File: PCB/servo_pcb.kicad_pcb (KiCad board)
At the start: 2 copper layers, 35 x 16 mm, 42 parts, among them J1 power in, M1 M1, M2 M2, U1 MM32G0001, U2 SL7533-3, U3 BDR6121H, U4 INA180A2, U5 AS5600

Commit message: cleaned up older pcbs and updated the master pcb
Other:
- board text added: "μDrive_1.0"
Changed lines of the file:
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@@
+		)
+	)
+	(gr_text "μDrive_1.0\n"
+		(at 75.5 33.6 0)
+		(layer "B.SilkS")
+		(effects
+			(font
+				(size 1.5 1.5)
+				(thickness 0.2)
+			)
+			(justify left bottom mirror)
 		)
 	)

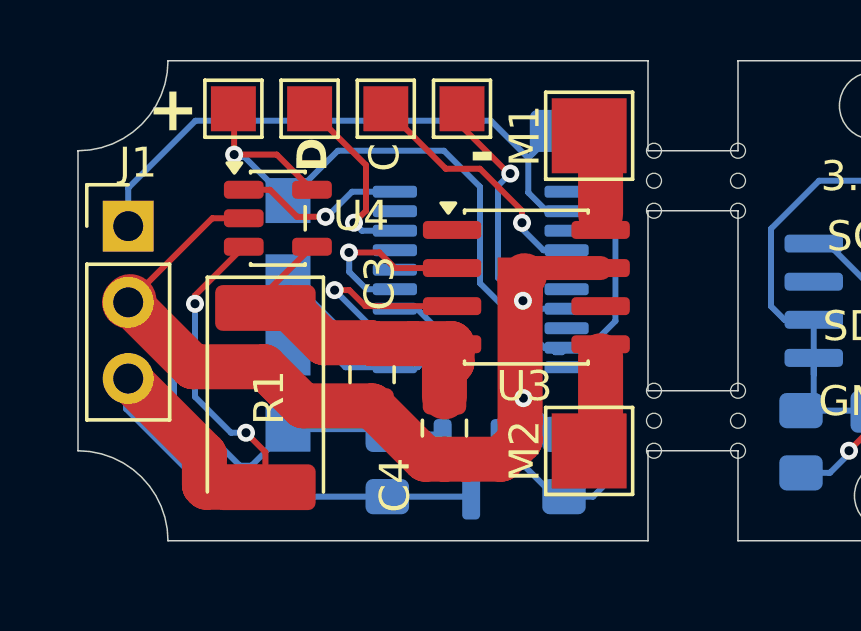
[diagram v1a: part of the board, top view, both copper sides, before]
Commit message: updated pcb:added ground pours
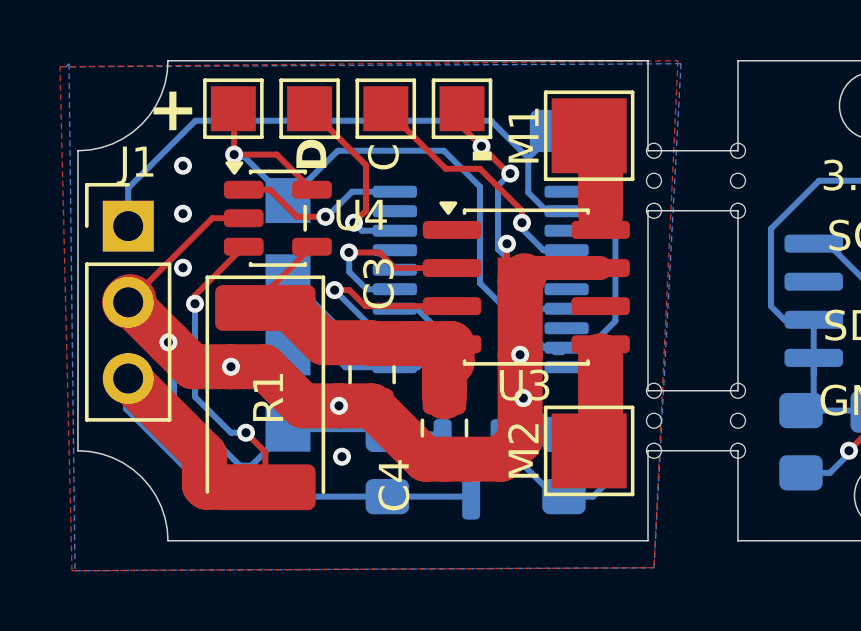
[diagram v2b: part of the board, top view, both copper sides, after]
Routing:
- net GND: track 55.8 -> 56.4 mm, vias 3 -> 12
- added copper zone on B.Cu, net GND
- added copper zone on F.Cu, net GND
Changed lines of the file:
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@@
 		)
 		(fp_text user "${REFERENCE}"
-			(at 8.2 -14.17175 90)
+			(at 0 -0.1 90)
 			(layer "B.Fab")
 			(effects
@@
 		)
 		(property "Value" "10K"
-			(at 11 -3.65 0)
+			(at 0 -0.1 0)
 			(layer "B.Fab")
 			(effects
@@
 	)
 	(gr_text ".\n"
-		(at 58.694 42.504 0)
+		(at 69.7 40.9 0)
 		(layer "B.SilkS")
 		(effects
@@
 	)
 	(segment
-		(start 75.231515 38.799485)
-		(end 75.497752 38.533248)
-		(width 0.8)
-		(layer "F.Cu")
-		(net 2)
-	)
-	(segment
-		(start 75.497752 38.533248)
-		(end 75.497752 38.179752)
-		(width 0.8)
+		(start 74.7 37.382)
+		(end 75.282 37.964)
+		(width 0.2)
 		(layer "F.Cu")
 		(net 2)
@@
 	(segment
 		(start 75.137 42.79)
-		(end 75.137 38.109)
+		(end 75.137 40.6)
 		(width 1.5)
 		(layer "F.Cu")
@@
 	)
 	(segment
+		(start 73.85 33.65)
+		(end 74.8 34.6)
+		(width 0.2)
+		(layer "F.Cu")
+		(net 2)
+	)
+	(segment
 		(start 62.074 38.853)
 		(end 62.080999 38.853)
@@
 	(segment
 		(start 67.9035 42.3035)
-		(end 70.202 42.3035)
+		(end 69.1 42.3035)
 		(width 1.5)
 		(layer "F.Cu")
@@
 	(segment
 		(start 64.227999 41)
-		(end 66.6 41)
+		(end 65.5 41)
 		(width 1.5)
 		(layer "F.Cu")
@@
 	)
 	(segment
-		(start 75.497752 38.179752)
-		(end 75.282 37.964)
-		(width 0.8)
+		(start 63.413999 40.186001)
+		(end 64.227999 41)
+		(width 1.5)
+		(layer "F.Cu")
+		(net 2)
+	)
+	(segment
+		(start 69.1 42.3035)
+		(end 70.202 42.3035)
+		(width 1.5)
 		(layer "F.Cu")
 		(net 2)
@@
 	(segment
 		(start 73.2 33)
-		(end 74.8 34.6)
+		(end 73.85 33.65)
 		(width 0.2)
 		(layer "F.Cu")
@@
 	)
 	(segment
+		(start 75.137 40.6)
+		(end 75.137 38.109)
+		(width 1.5)
+		(layer "F.Cu")
+		(net 2)
+	)
+	(segment
+		(start 74.7 36.9)
+		(end 74.7 37.382)
+		(width 0.2)
+		(layer "F.Cu")
+		(net 2)
+	)
+	(segment
 		(start 62.080999 38.853)
-		(end 64.227999 41)
+		(end 63.413999 40.186001)
 		(width 1.5)
 		(layer "F.Cu")
@@
 	)
 	(segment
+		(start 65.5 41)
+		(end 66.6 41)
+		(width 1.5)
+		(layer "F.Cu")
+		(net 2)
+	)
+	(segment
 		(start 74.8 34.6)
 		(end 74.809 34.591)
@@
 	)
 	(via
-		(at 75.231515 38.799485)
+		(at 69.2 44)
 		(size 0.6)
 		(drill 0.3)
 		(layers "F.Cu" "B.Cu")
+		(free yes)
+		(net 2)
+	)
+	(via
+		(at 69.1 42.3035)
+		(size 0.6)
+		(drill 0.3)
+		(layers "F.Cu" "B.Cu")
+		(net 2)
+	)
+	(via
+		(at 63.9 34.3)
+		(size 0.6)
+		(drill 0.3)
+		(layers "F.Cu" "B.Cu")
+		(free yes)
+		(net 2)
+	)
+	(via
+		(at 63.9 37.7)
+		(size 0.6)
+		(drill 0.3)
+		(layers "F.Cu" "B.Cu")
+		(free yes)
 		(net 2)
 	)
@@
 	)
 	(via
+		(at 65.5 41)
+		(size 0.6)
+		(drill 0.3)
+		(layers "F.Cu" "B.Cu")
+		(net 2)
+	)
+	(via
+		(at 74.7 36.9)
+		(size 0.6)
+		(drill 0.3)
+		(layers "F.Cu" "B.Cu")
+		(net 2)
+	)
+	(via
 		(at 75.245722 42.045722)
 		(size 0.6)
@@
 		(net 2)
 	)
+	(via
+		(at 73.85 33.65)
+		(size 0.6)
+		(drill 0.3)
+		(layers "F.Cu" "B.Cu")
+		(net 2)
+	)
+	(via
+		(at 75.137 40.6)
+		(size 0.6)
+		(drill 0.3)
+		(layers "F.Cu" "B.Cu")
+		(net 2)
+	)
+	(via
+		(at 63.9 35.9)
+		(size 0.6)
+		(drill 0.3)
+		(layers "F.Cu" "B.Cu")
+		(free yes)
+		(net 2)
+	)
+	(via
+		(at 63.413999 40.186001)
+		(size 0.6)
+		(drill 0.3)
+		(layers "F.Cu" "B.Cu")
+		(net 2)
+	)
 	(segment
 		(start 75.245722 42.045722)
@@
 	)
 	(segment
-		(start 75.231515 38.799485)
-		(end 75.49803 39.066)
+		(start 74.4 37.082)
+		(end 74.518 37.082)
 		(width 0.2)
 		(layer "B.Cu")
@@
 	)
 	(segment
-		(start 74.4 38.032)
-		(end 74.4 34.969472)
+		(start 63.6 42.1)
+		(end 63.6 40.379)
 		(width 0.2)
 		(layer "B.Cu")
@@
 	)
 	(segment
-		(start 63.6 42.1)
-		(end 63.6 40.379)
+		(start 75.282 37.964)
+		(end 74.4 37.082)
 		(width 0.2)
 		(layer "B.Cu")
@@
 	)
 	(segment
+		(start 75.282 37.964)
+		(end 75.282 38.84997)
+		(width 0.2)
+		(layer "B.Cu")
+		(net 2)
+	)
+	(segment
 		(start 72.327 43.255)
 		(end 72.554 43.482)
@@
 	)
 	(segment
-		(start 67.4 43.08)
-		(end 66.18 44.3)
+		(start 75.282 38.84997)
+		(end 75.49803 39.066)
 		(width 0.2)
 		(layer "B.Cu")
@@
 	)
 	(segment
-		(start 75.167485 38.799485)
-		(end 74.4 38.032)
+		(start 67.4 43.08)
+		(end 66.18 44.3)
 		(width 0.2)
 		(layer "B.Cu")
@@
 	)
 	(segment
-		(start 76.455 43.255)
-		(end 76.6 43.255)
+		(start 74.4 37.082)
+		(end 74.4 34.969472)
 		(width 0.2)
 		(layer "B.Cu")
@@
 	)
 	(segment
-		(start 70.535 43.08)
-		(end 70.71 43.255)
+		(start 74.4 34.969472)
+		(end 74.809 34.560472)
 		(width 0.2)
 		(layer "B.Cu")
@@
 	)
 	(segment
-		(start 75.231515 38.799485)
-		(end 75.167485 38.799485)
+		(start 76.455 43.255)
+		(end 76.6 43.255)
 		(width 0.2)
 		(layer "B.Cu")
@@
 	)
 	(segment
-		(start 74.4 34.969472)
-		(end 74.809 34.560472)
+		(start 70.535 43.08)
+		(end 70.71 43.255)
 		(width 0.2)
 		(layer "B.Cu")
@@
 	)
 	(segment
+		(start 74.518 37.082)
+		(end 74.7 36.9)
+		(width 0.2)
+		(layer "B.Cu")
+		(net 2)
+	)
+	(segment
 		(start 65.605044 32.425044)
 		(end 65.58 32.4)
@@
 		(net 30)
 	)
+	(zone
+		(net 2)
+		(net_name "GND")
+		(layer "F.Cu")
+		(hatch edge 0.5)
+		(connect_pads
+			(clearance 0.5)
+		)
+		(min_thickness 0.25)
+		(filled_areas_thickness no)
+		(fill yes
+			(thermal_gap 0.5)
+			(thermal_bridge_width 0.5)
+		)
+		(polygon
+			(pts
+				(xy 59.8 31) (xy 80.4 30.8) (xy 79.6 47.7) (xy 60.2 47.8)
+			)
+		)
+	)
+	(zone
+		(net 2)
+		(net_name "GND")
+		(layer "B.Cu")
+		(hatch edge 0.5)
+		(priority 1)
+		(connect_pads
+			(clearance 0.5)
+		)
+		(min_thickness 0.25)
+		(filled_areas_thickness no)
+		(fill yes
+			(thermal_gap 0.5)
+			(thermal_bridge_width 0.5)
+		)
+		(polygon
+			(pts
+				(xy 60.1 30.9) (xy 60.3 47.8) (xy 79.6 47.7) (xy 80.5 30.9) (xy 60 31)
+			)
+		)
+	)
 	(group ""

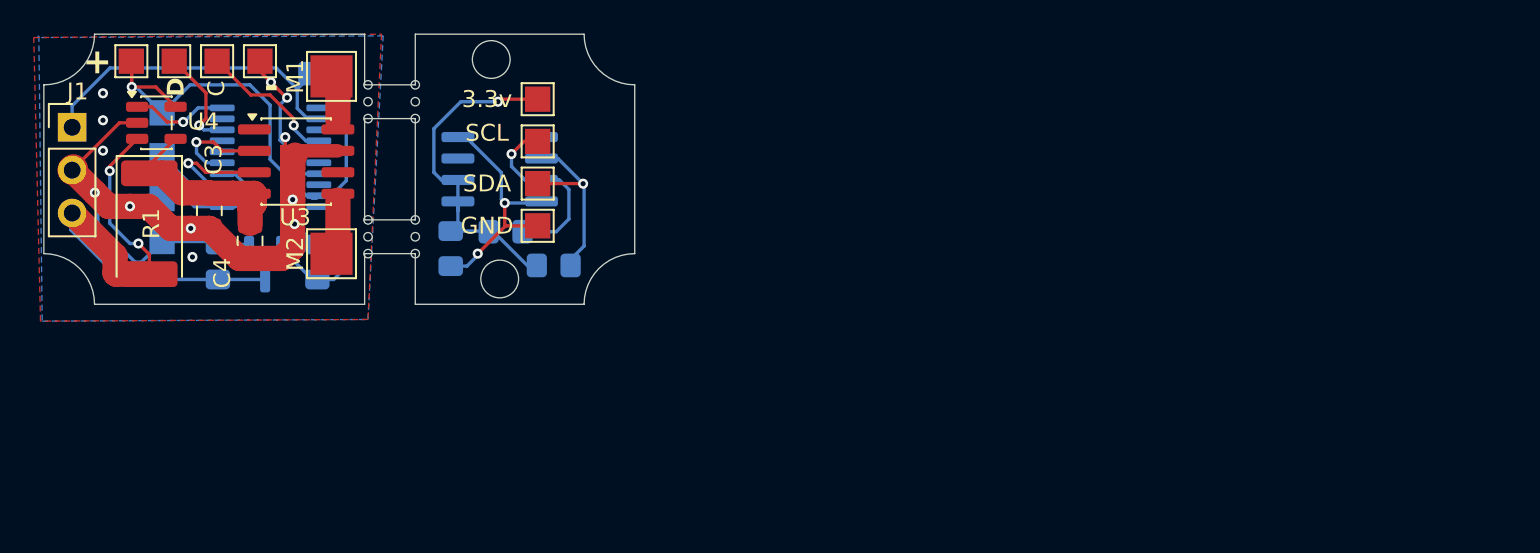
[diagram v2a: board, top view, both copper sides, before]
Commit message: updated  the pcb for generic motors
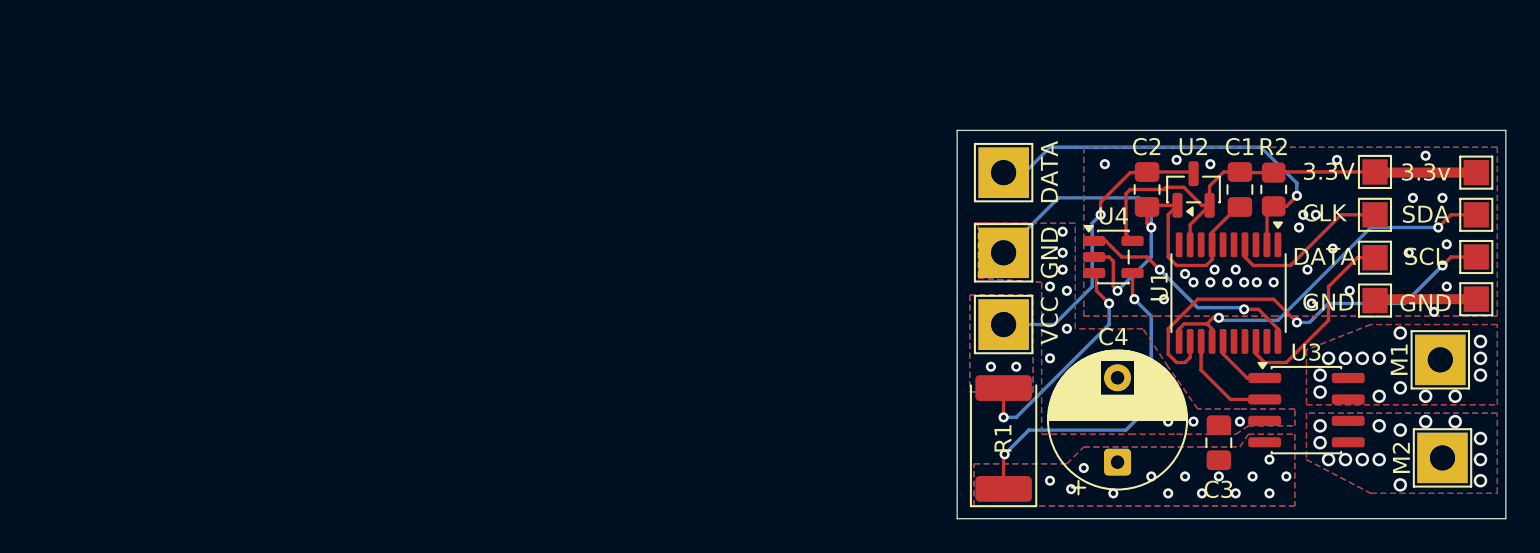
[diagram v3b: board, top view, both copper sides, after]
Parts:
- removed ? (x13): , 
- removed C5: 100nf, Capacitor_SMD:C_0805_2012Metric_Pad1.18x1.45mm_HandSolder
- removed J1: power in, Connector_PinHeader_2.54mm:PinHeader_1x03_P2.54mm_Vertical
- removed R3, R4: 10K, Resistor_SMD:R_0805_2012Metric_Pad1.20x1.40mm_HandSolder
- removed TP1: 3.3v, TestPoint:TestPoint_Pad_1.5x1.5mm
- removed TP11: SDA, TestPoint:TestPoint_Pad_1.5x1.5mm
- removed TP12: SCL, TestPoint:TestPoint_Pad_1.5x1.5mm
- removed TP2: GND, TestPoint:TestPoint_Pad_1.5x1.5mm
- removed U5: AS5600, Package_SO:SOIC-8_3.9x4.9mm_P1.27mm
- added G***: LOGO, LOGO, B.Cu at (130.8, 51.5)
- added M3: VCC, TestPoint:TestPoint_THTPad_3.0x3.0mm_Drill1.5mm, F.Cu at (117.2, 48.0)
- added M4: GND, TestPoint:TestPoint_THTPad_3.0x3.0mm_Drill1.5mm, F.Cu at (117.2, 43.8)
- added M5: DATA, TestPoint:TestPoint_THTPad_3.0x3.0mm_Drill1.5mm, F.Cu at (117.2, 39.0)
- added REF**: OSHW-Logo_5.7x6mm_SilkScreen, Symbol:OSHW-Logo_5.7x6mm_SilkScreen, B.Cu at (118.2, 55.0)
- C1, C2, R2, TP10, TP7, TP8, TP9, U1, U2: moved to F.Cu
- C4: value 10uf -> 470uf; footprint Capacitor_SMD:C_0805_2012Metric_Pad1.18x1.45mm_HandSolder -> Capacitor_THT:CP_Radial_D8.0mm_P5.00mm
- M1, M2: footprint TestPoint:TestPoint_Pad_2.5x2.5mm -> TestPoint:TestPoint_THTPad_3.0x3.0mm_Drill1.5mm
- TP3: value SWCLK -> CLK
- TP4: value -VE -> GND
- TP5: value +VE -> 3.3V
- TP6: value SWIO -> DATA
- U3: value BDR6121H -> CP2119L
- moved TP9 78.1 mm to (145.2, 44.0)
- moved TP7 77.9 mm to (145.2, 39.0)
- moved TP8 77.9 mm to (145.2, 41.5)
- moved TP5 74.0 mm to (139.2, 39.0), turned to -90 degrees
- moved TP4 73.4 mm to (145.2, 46.5)
- moved TP6 72.1 mm to (139.2, 44.0)
- moved TP10 71.9 mm to (139.2, 46.6)
- moved TP3 69.2 mm to (139.2, 41.5)
- moved M1 67.8 mm to (143.1, 50.1)
- moved M2 66.9 mm to (143.2, 55.9)
- moved U3 61.6 mm to (135.2, 53.1)
- moved C3 61.4 mm to (130.0, 55.0), turned to 90 degrees
- moved U1 57.3 mm to (130.6, 46.1), turned to -90 degrees
- moved U4 57.2 mm to (123.8, 44.0)
- moved R2 56.6 mm to (133.2, 40.0), turned to -90 degrees
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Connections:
- M1 pad 1: Net-(U3-OUTA) -> Net-(M1-Pad1)
- M2 pad 1: Net-(U3-OUTB) -> Net-(M2-Pad1)
- U3 pad 1: unconnected-(U3-NC-Pad1) -> /INB
- U3 pad 2: /INB -> /INA
- U3 pad 3: /INA -> GND
- U3 pad 5: Net-(U3-OUTB) -> Net-(M2-Pad1)
- U3 pad 6: unconnected-(U3-NC-Pad6) -> Net-(M2-Pad1)
- U3 pad 7: GND -> Net-(M1-Pad1)
- U3 pad 8: Net-(U3-OUTA) -> Net-(M1-Pad1)
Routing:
- net Net-(U5-VDD3V3): track 21.3 -> 0.00 mm, vias 1 -> 0
- net /SCL: track 4.54 -> 25.2 mm, vias 0 -> 2
- net GND: track 56.4 -> 38.4 mm, vias 12 -> 45
- net Net-(U5-DIR): track 15.1 -> 0.00 mm, vias 2 -> 0
- net /Angle: track 7.64 -> 22.5 mm, vias 0 -> 2
- net +3.3V: track 40.8 -> 28.7 mm, vias 1 -> 0
- net Net-(U5-SCL): track 11.4 -> 0.00 mm, vias 1 -> 0
- net Net-(U5-SDA): track 11.1 -> 0.00 mm, vias 1 -> 0
- net /DRIVER VCC: track 12.0 -> 19.9 mm, vias 0 -> 16
- net /Current Read: track 6.01 -> 13.9 mm, vias 1 -> 2
- net Net-(U1-PA13/SWDIO): track 6.22 -> 11.7 mm, vias 1 -> 0
- net Net-(U3-OUTB): track 3.33 -> 0.00 mm
- net Net-(U3-OUTA): track 2.83 -> 0.00 mm
- net /DATA: track 21.1 -> 23.7 mm, vias 0 -> 1
- net /INB: track 6.06 -> 3.79 mm, vias 1 -> 0
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- added copper zone on B.Cu, net /DRIVER VCC
- added copper zone on F.Cu, net /DRIVER VCC
- added copper zone on B.Cu, net Net-(M1-Pad1)
- added copper zone on F.Cu, net Net-(M1-Pad1)
- added copper zone on B.Cu, net Net-(M2-Pad1)
- added copper zone on F.Cu, net Net-(M2-Pad1)
- added copper zone on B.Cu, net VCC
- added copper zone on F.Cu, net VCC
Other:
- board size 35 x 16 mm -> 32.5 x 23 mm
- board text added: "Vin:5-18v 5A"
- board text added: "μDrive_v1.0"
- board text removed: "+"
- board text removed: "-"
- board text removed: "."
- board text removed: "C"
- board text removed: "D"
- board text removed: "μDrive_1.0"

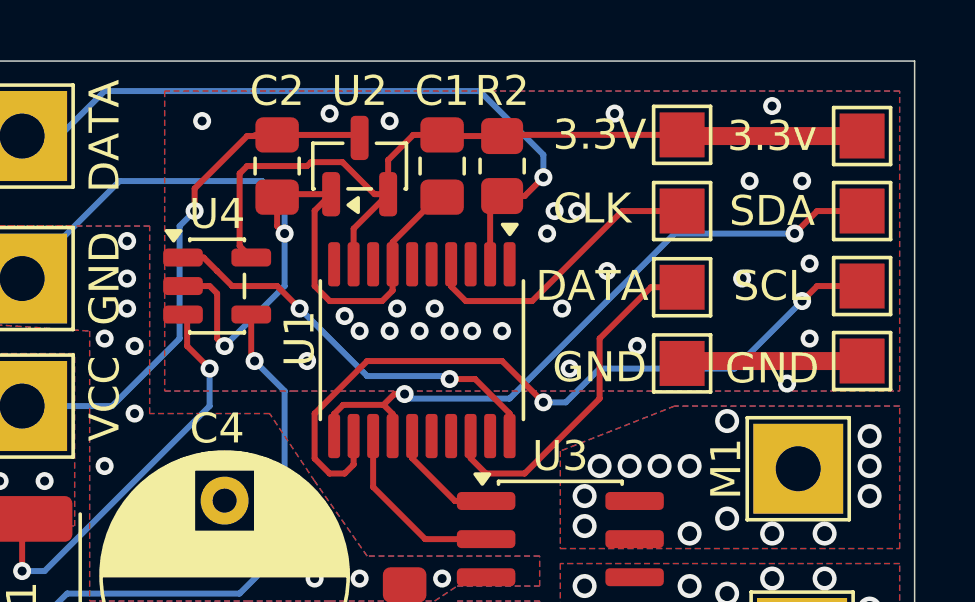
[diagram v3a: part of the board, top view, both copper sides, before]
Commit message: fix: add hardware watchdog (IWDG) and disable debug UART from ISR context
    - Enable IWDG with ~500ms timeout for automatic MCU recovery when
      main loop hangs (no manual reset or power cycle needed)
    - Set DEBUG_LOG=0 to eliminate SysTick/UART race condition where
      print_status() from pid_update() could preempt send_status_reply()
      mid-transmission, permanently deadlocking the UART in RX mode
    - Add PA11 reset button footprint to PCB
    - Rewrite docs/troubleshoot.md with practical symptom-to-fix format
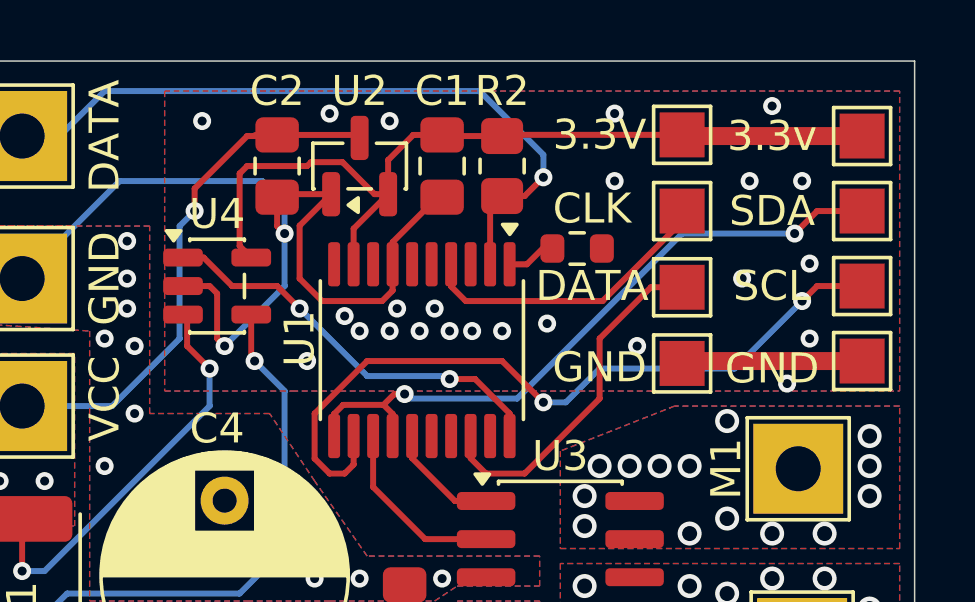
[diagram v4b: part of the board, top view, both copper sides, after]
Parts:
- added R3: R_0603_1608Metric, Resistor_SMD:R_0603_1608Metric, F.Cu at (135.8, 42.8)
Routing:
- net unconnected-(U1-PA11-Pad1): track 0.00 -> 1.67 mm
- net GND: track 38.4 -> 39.3 mm, vias 45 -> 41
